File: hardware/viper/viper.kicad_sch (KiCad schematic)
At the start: 303 parts, among them J1 USB_B_Mini, Q1 2N7002, SW1 Cherry Alps Hybrid, SW10 Cherry Alps Hybrid, SW11 Cherry Alps Hybrid, SW12 Cherry Alps Hybrid, SW13 Cherry Alps Hybrid, SW14 Cherry Alps Hybrid, SW14_1 Cherry Alps Hybrid, SW15 Cherry Alps Hybrid, SW16 Cherry Alps Hybrid, SW17 Cherry Alps Hybrid, SW18 Cherry Alps Hybrid, SW19 Cherry Alps Hybrid, SW2 Cherry Alps Hybrid, SW20 Cherry Alps Hybrid, SW21 Cherry Alps Hybrid, SW22 Cherry Alps Hybrid, SW23 Cherry Alps Hybrid, SW24 Cherry Alps Hybrid, SW25 Cherry Alps Hybrid, SW26 Cherry Alps Hybrid, SW27 Cherry Alps Hybrid, SW28 Cherry Alps Hybrid, SW28_1 Cherry Alps Hybrid, SW29 Cherry Alps Hybrid, SW29_1 Cherry Alps Hybrid, SW3 Cherry Alps Hybrid, SW30 Cherry Alps Hybrid, SW31 Cherry Alps Hybrid, SW32 Cherry Alps Hybrid, SW33 Cherry Alps Hybrid, SW34 Cherry Alps Hybrid, SW35 Cherry Alps Hybrid, SW36 Cherry Alps Hybrid, SW37 Cherry Alps Hybrid, SW38 Cherry Alps Hybrid, SW39 Cherry Alps Hybrid, SW4 Cherry Alps Hybrid, SW40 Cherry Alps Hybrid, SW41 Cherry Alps Hybrid, SW41_1 Cherry Alps Hybrid, SW42 Cherry Alps Hybrid, SW43 Cherry Alps Hybrid, SW43_1 Cherry Alps Hybrid, SW44 Cherry Alps Hybrid, SW45 Cherry Alps Hybrid, SW46 Cherry Alps Hybrid, SW47 Cherry Alps Hybrid, SW48 Cherry Alps Hybrid, SW49 Cherry Alps Hybrid, SW5 Cherry Alps Hybrid, SW50 Cherry Alps Hybrid, SW51 Cherry Alps Hybrid, SW52 Cherry Alps Hybrid, SW53 Cherry Alps Hybrid, SW54 Cherry Alps Hybrid, SW55 Cherry Alps Hybrid, SW55_1 Cherry Alps Hybrid, SW56 Cherry Alps Hybrid, SW57 Cherry Alps Hybrid, SW58 Cherry Alps Hybrid, SW59 Cherry Alps Hybrid, SW6 Cherry Alps Hybrid, SW60 Cherry Alps Hybrid, SW61 Cherry Alps Hybrid, SW7 Cherry Alps Hybrid, SW8 Cherry Alps Hybrid, SW9 Cherry Alps Hybrid, U1 ATmega32U4-A, U2 PRTR5V0U2X, Y1 Crystal_GND24

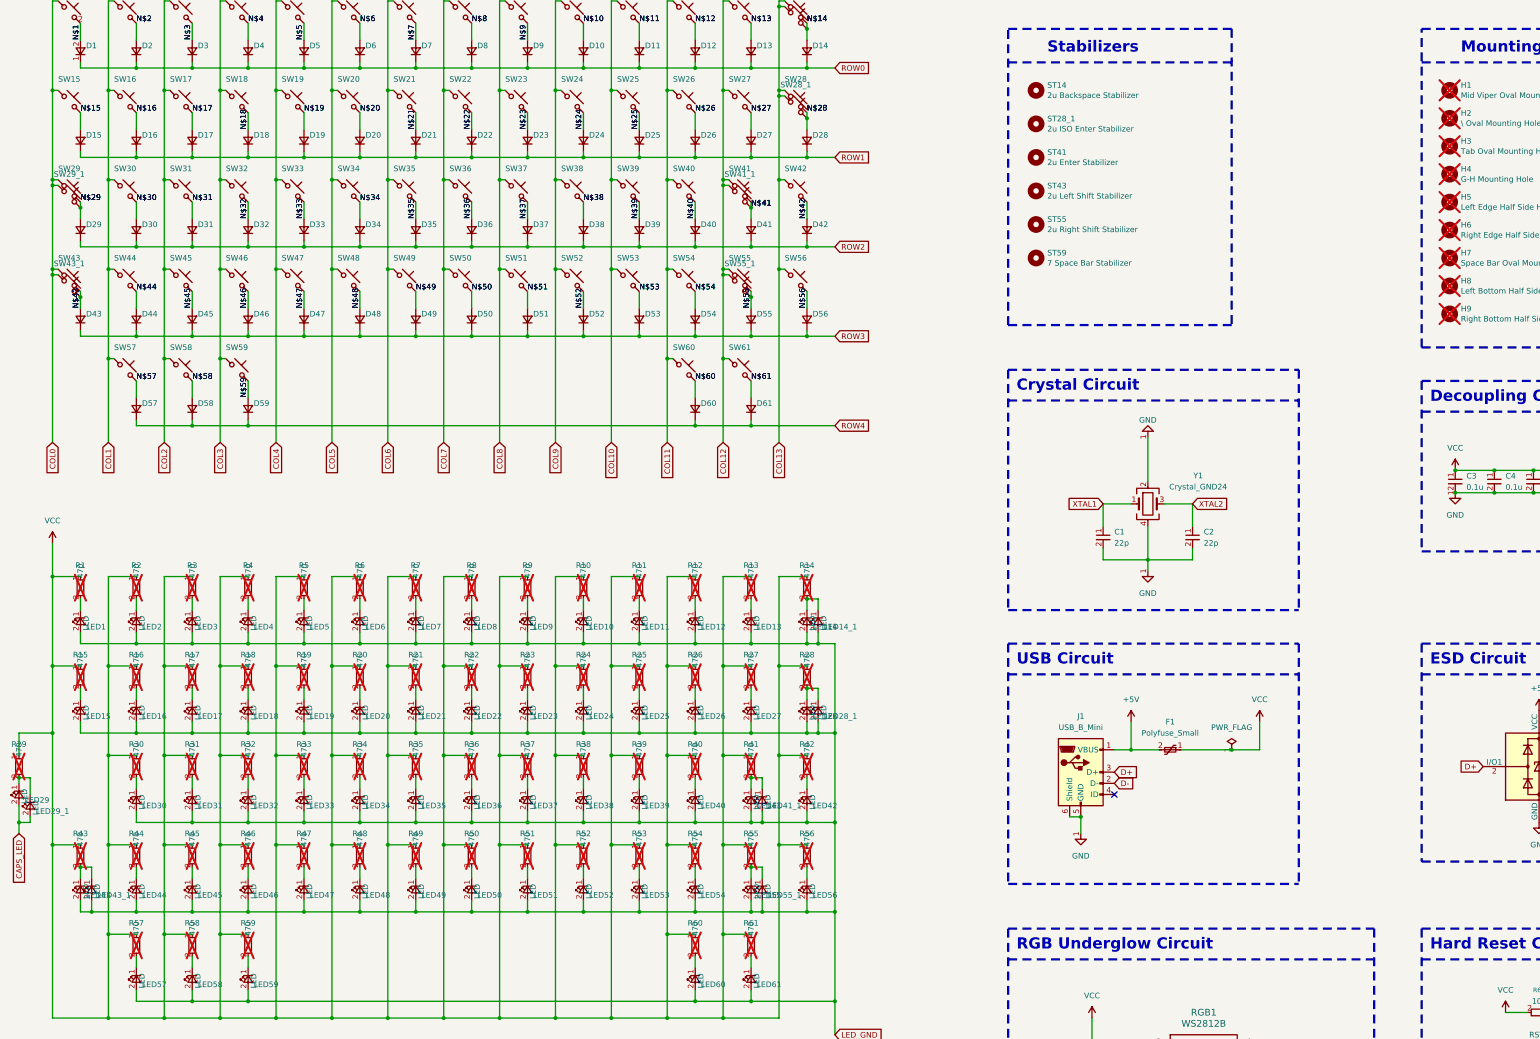
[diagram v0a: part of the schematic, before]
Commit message: Included schematic.svg in README
Removed DNP flags
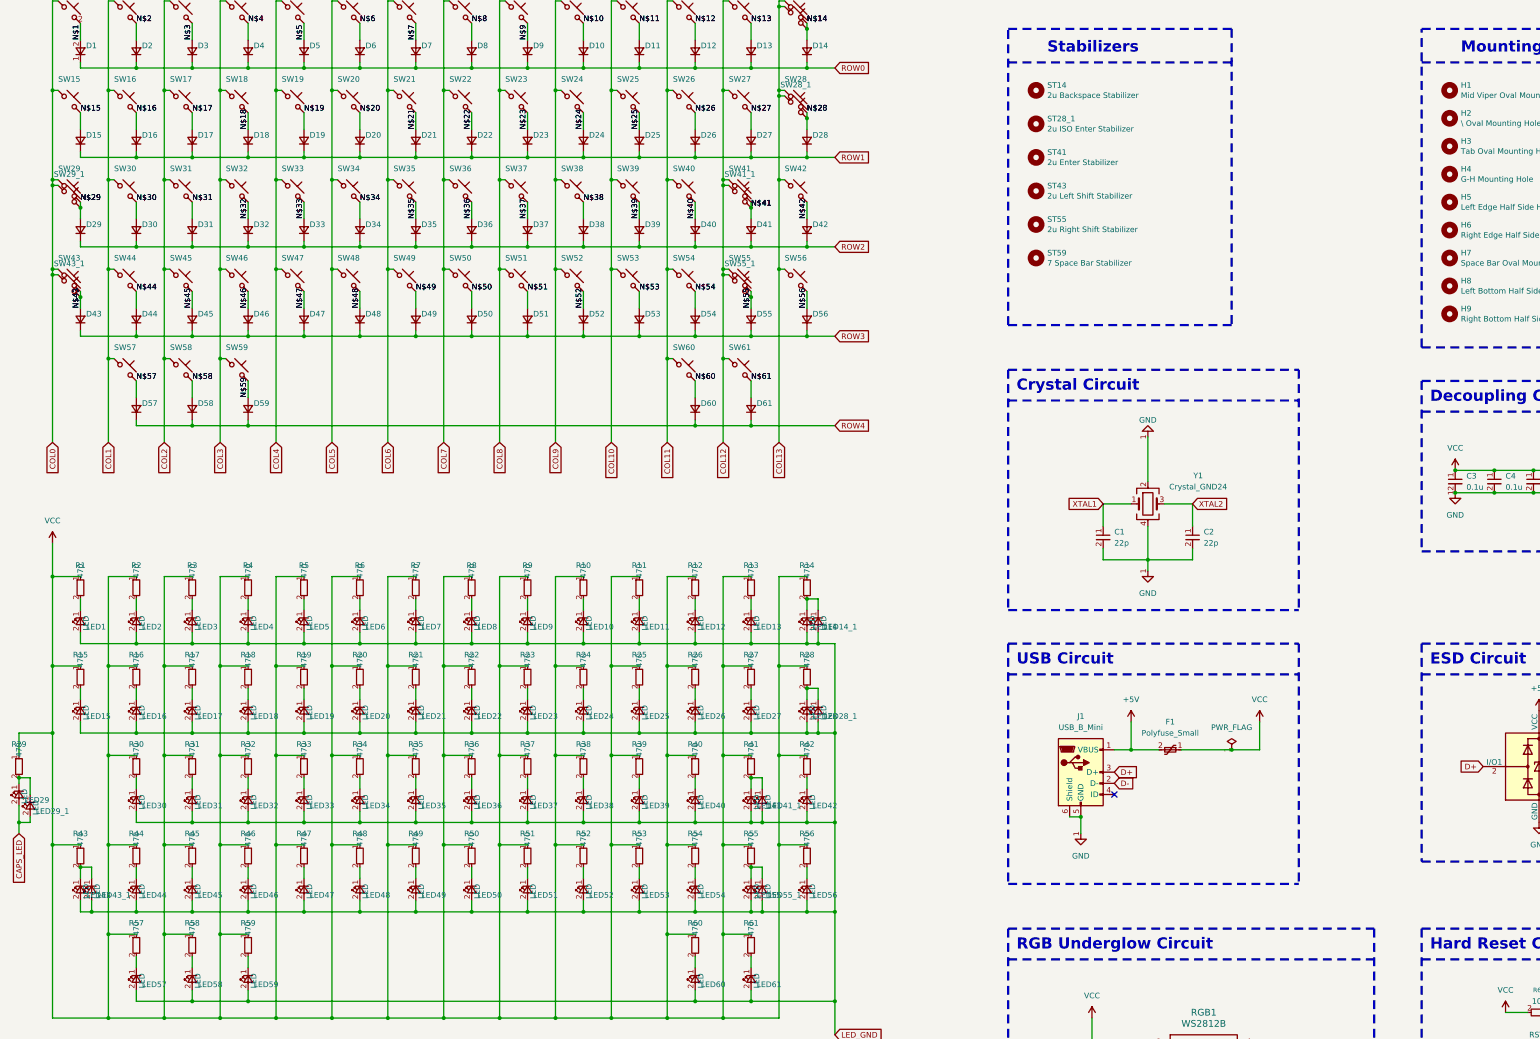
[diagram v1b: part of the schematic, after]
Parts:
- H1, H2, H3, H4, H5, H6, H7, H8, H9, R1, R10, R11, R12, R13, R14, R15, R16, R17, R18, R19, R2, R20, R21, R22, R23, R24, R25, R26, R27, R28, R29, R3, R30, R31, R32, R33, R34, R35, R36, R37, R38, R39, R4, R40, R41, R42, R43, R44, R45, R46, R47, R48, R49, R5, R50, R51, R52, R53, R54, R55, R56, R57, R58, R59, R6, R60, R61, R7, R8, R9: now fitted

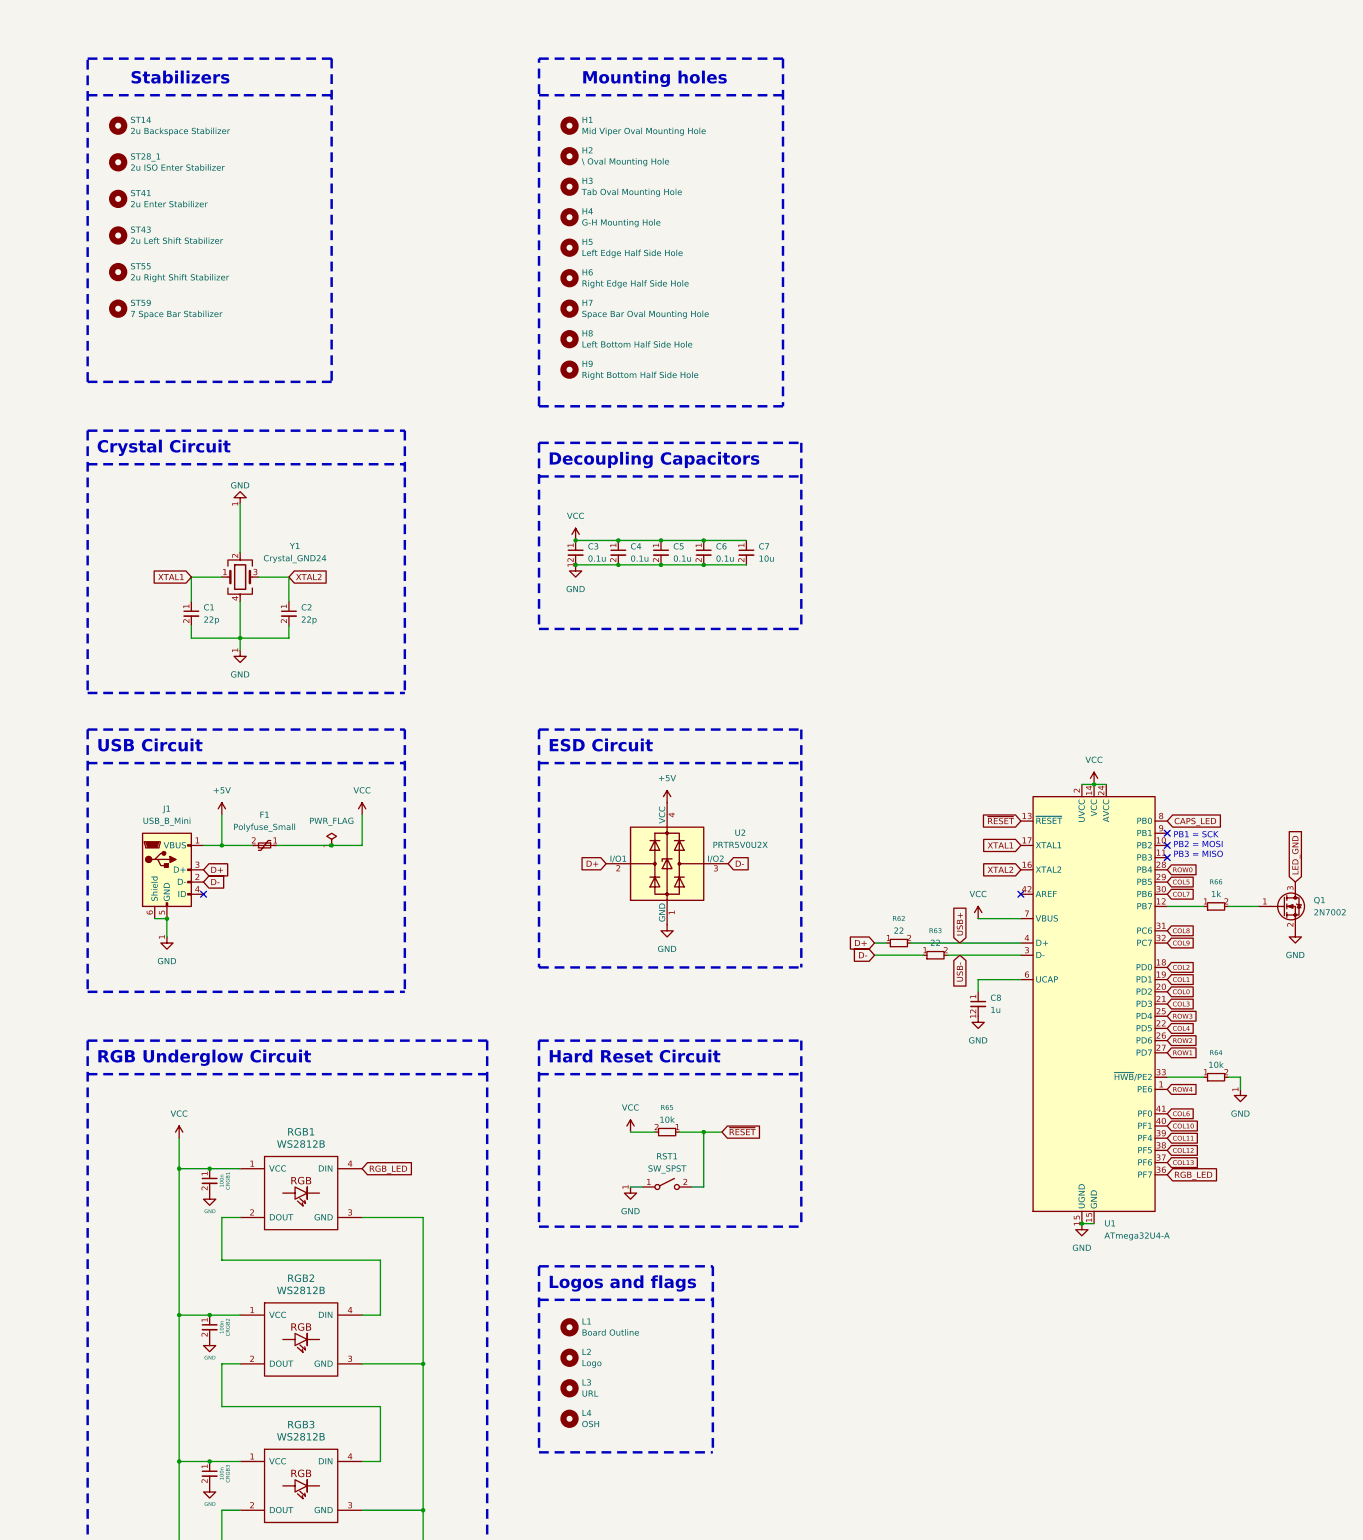
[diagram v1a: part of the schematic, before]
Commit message: Updated docs
Updated schematic & changed DSOD123F to 0805 footprints where needed
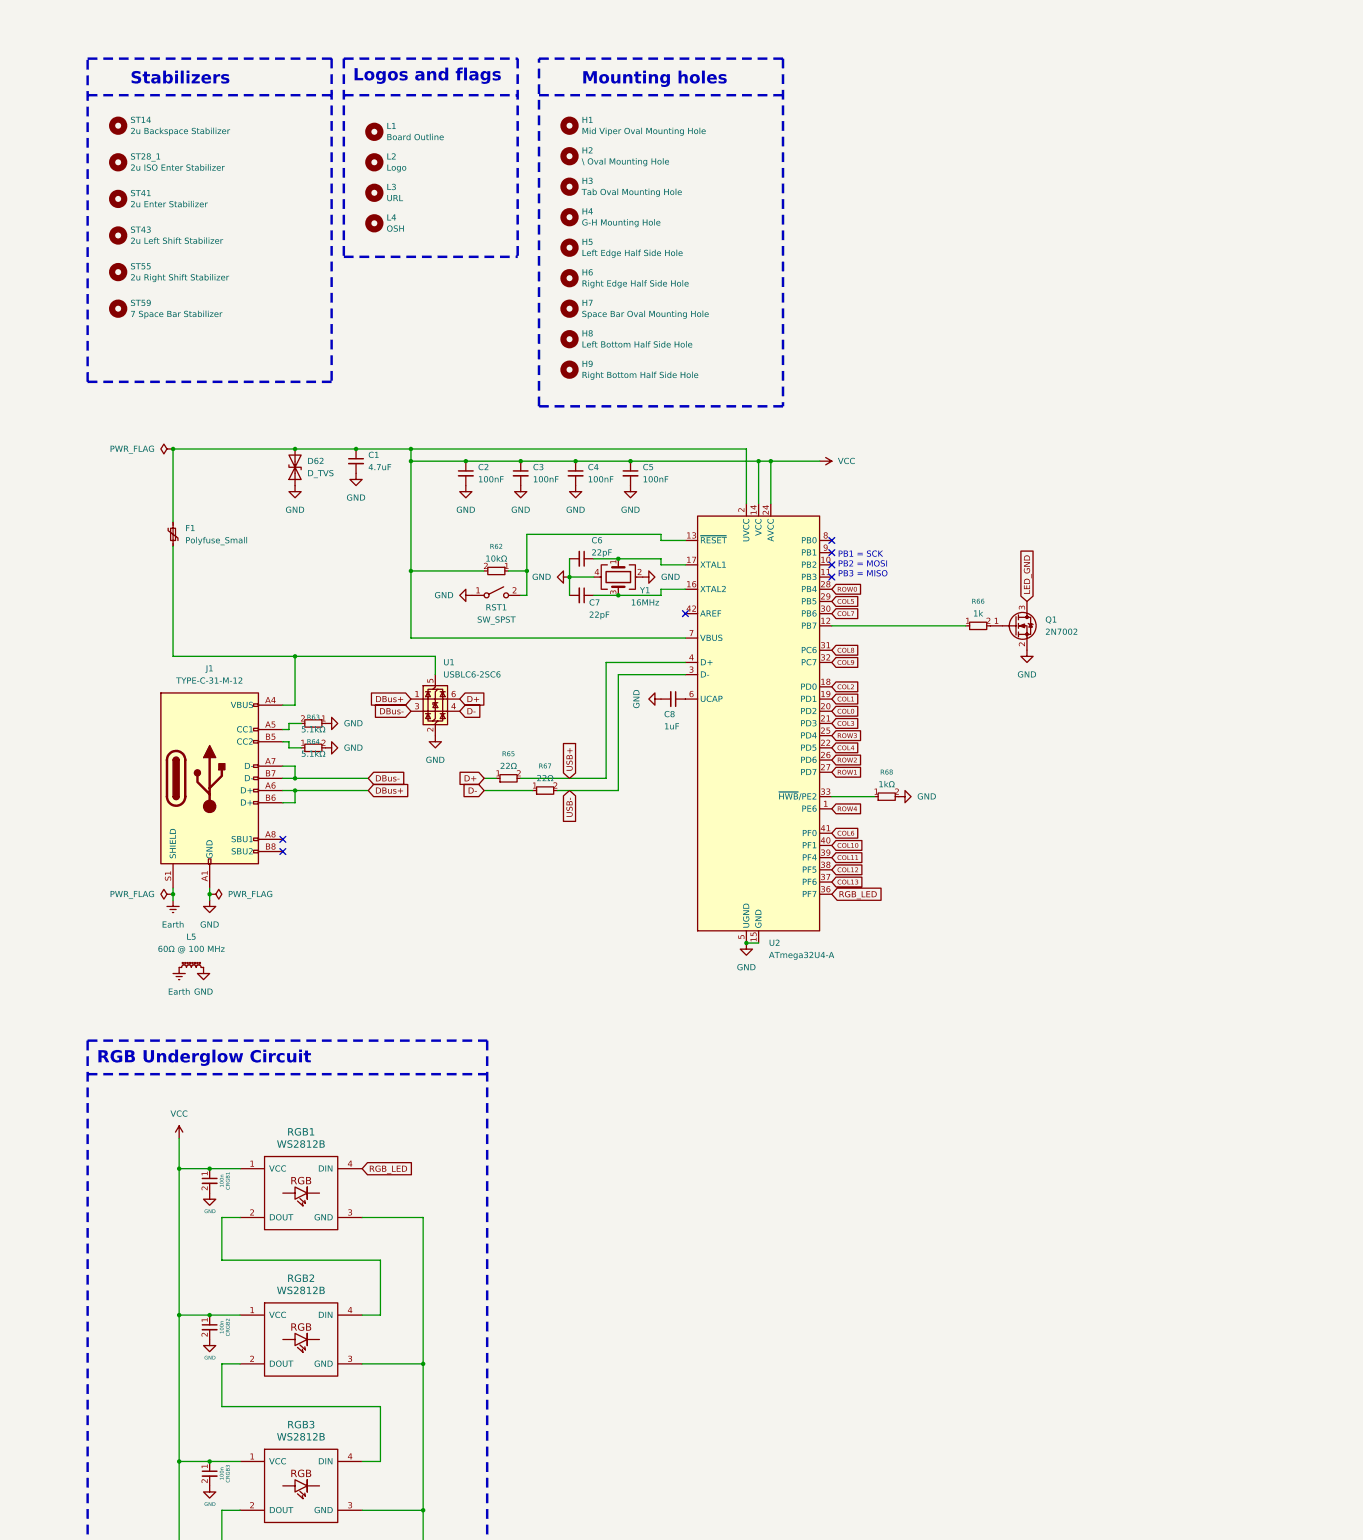
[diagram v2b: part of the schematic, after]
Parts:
- removed C2: 22p, Capacitor_SMD:C_0603_1608Metric, symbol Device:C_Small
- removed J1: USB_B_Mini, acheron_Connectors:USB_MiniB_Hirose_UX60-MB-5S8, symbol Connector:USB_B_Mini
- removed U2: PRTR5V0U2X, Package_TO_SOT_SMD:SOT-143, symbol Power_Protection:PRTR5V0U2X
- added C7: 22pF, Capacitor_SMD:C_0805_2012Metric_Pad1.18x1.45mm_HandSolder, symbol Device:C_Small
- added D62: D_TVS, Diode_SMD:D_0805_2012Metric_Pad1.15x1.40mm_HandSolder, symbol Device:D_TVS
- added J1: TYPE-C-31-M-12, Connector_USB:USB_C_Receptacle_HRO_TYPE-C-31-M-12, symbol Connector:USB_C_Receptacle_USB2.0_16P
- added L5: 60Ω @ 100 MHz, Inductor_SMD:L_1206_3216Metric_Pad1.42x1.75mm_HandSolder, symbol Device:L_Ferrite_Small
- added R67: 22Ω, Resistor_SMD:R_0805_2012Metric_Pad1.20x1.40mm_HandSolder, symbol Device:R_Small
- added R68: 1kΩ, Resistor_SMD:R_0805_2012Metric_Pad1.20x1.40mm_HandSolder, symbol Device:R_Small
- added U1: USBLC6-2SC6, Package_TO_SOT_SMD:SOT-23-6, symbol Power_Protection:USBLC6-2SC6
- C1: renamed from C3; value 0.1u -> 4.7uF; footprint Capacitor_SMD:C_0603_1608Metric -> Capacitor_SMD:C_0805_2012Metric_Pad1.18x1.45mm_HandSolder; LCSC (none) -> C36911366
- C2: renamed from C4; value 0.1u -> 100nF; footprint Capacitor_SMD:C_0603_1608Metric -> Capacitor_SMD:C_0805_2012Metric_Pad1.18x1.45mm_HandSolder; LCSC (none) -> C36911366
- C3: renamed from C5; value 0.1u -> 100nF; footprint Capacitor_SMD:C_0603_1608Metric -> Capacitor_SMD:C_0805_2012Metric_Pad1.18x1.45mm_HandSolder; LCSC (none) -> C36911366
- C4: renamed from C6; value 0.1u -> 100nF; footprint Capacitor_SMD:C_0603_1608Metric -> Capacitor_SMD:C_0805_2012Metric_Pad1.18x1.45mm_HandSolder; LCSC (none) -> C36911366
- C5: renamed from C7; value 10u -> 100nF; footprint Capacitor_SMD:C_0603_1608Metric -> Capacitor_SMD:C_0805_2012Metric_Pad1.18x1.45mm_HandSolder; LCSC (none) -> C47117445
- C6: renamed from C1; value 22p -> 22pF; footprint Capacitor_SMD:C_0603_1608Metric -> Capacitor_SMD:C_0805_2012Metric_Pad1.18x1.45mm_HandSolder; LCSC (none) -> C22399635
- C8: value 1u -> 1uF; footprint Capacitor_SMD:C_0603_1608Metric -> Capacitor_SMD:C_0805_2012Metric_Pad1.18x1.45mm_HandSolder; LCSC (none) -> C5254818
- D1, D10, D11, D12, D13, D14, D15, D16, D17, D18, D19, D2, D20, D21, D22, D23, D24, D25, D26, D27, D28, D29, D3, D30, D31, D32, D33, D34, D35, D36, D37, D38, D39, D4, D40, D41, D42, D43, D44, D45, D46, D47, D48, D49, D5, D50, D51, D52, D53, D54, D55, D56, D57, D58, D59, D6, D60, D61, D7, D8, D9: footprint Diode_SMD:D_SOD-123F -> Diode_SMD:D_0805_2012Metric_Pad1.15x1.40mm_HandSolder
- F1: footprint Fuse:Fuse_1206_3216Metric -> Fuse:Fuse_0805_2012Metric_Pad1.15x1.40mm_HandSolder; LCSC (none) -> C70158; TODO (none) -> ${ERC_ERROR TODO} Calulate proper value
- R1, R10, R11, R12, R13, R14, R15, R16, R17, R18, R19, R2, R20, R21, R22, R23, R24, R25, R26, R27, R28, R29, R3, R30, R31, R32, R33, R34, R35, R36, R37, R38, R39, R4, R40, R41, R42, R43, R44, R45, R46, R47, R48, R49, R5, R50, R51, R52, R53, R54, R55, R56, R57, R58, R59, R6, R60, R61, R7, R8, R9: footprint Resistor_SMD:R_1206_3216Metric_Pad1.30x1.75mm_HandSolder -> Resistor_SMD:R_0815_2038Metric_Pad1.20x4.05mm_HandSolder
- R62: value 22 -> 10kΩ; footprint Resistor_SMD:R_0603_1608Metric -> Resistor_SMD:R_0805_2012Metric_Pad1.20x1.40mm_HandSolder; LCSC (none) -> C17414
- R63: value 22 -> 5.1kΩ; footprint Resistor_SMD:R_0603_1608Metric -> Resistor_SMD:R_0805_2012Metric_Pad1.20x1.40mm_HandSolder; LCSC (none) -> C27834
- R64: value 10k -> 5.1kΩ; footprint Resistor_SMD:R_0603_1608Metric -> Resistor_SMD:R_0805_2012Metric_Pad1.20x1.40mm_HandSolder; LCSC (none) -> C27834
- R65: value 10k -> 22Ω; footprint Resistor_SMD:R_0603_1608Metric -> Resistor_SMD:R_0805_2012Metric_Pad1.20x1.40mm_HandSolder; LCSC (none) -> C25295
- R66: footprint Resistor_SMD:R_0603_1608Metric -> Resistor_SMD:R_0815_2038Metric_Pad1.20x4.05mm_HandSolder
- RST1: LCSC (none) -> C92584
- U2: renamed from U1; footprint Package_QFP:TQFP-44_10x10mm_P0.8mm -> Package_DFN_QFN:QFN-44-1EP_7x7mm_P0.5mm_EP5.2x5.2mm
- Y1: value Crystal_GND24 -> 16MHz; LCSC (none) -> C255909
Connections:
- net +5V is gone; now on net VCC: F1.2
- net CAPS_LED: no longer U2.8 (PB0)
- net D+: now also R65.1, U1.6 (I/O1); no longer R62.1
- net D-: now also R67.1, U1.4 (I/O2); no longer R63.1
- net GND: now also R63.1, C7.2, D62.1 (A1), J1.A1 (GND), J1.A12 (GND), J1.B1 (GND), J1.B12 (GND), L5.2, R68.2, U1.2 (GND)
- net USB+: now also R65.2; no longer R62.2
- net USB-: now also R67.2; no longer R63.2
- net VCC: now also R62.2, D62.2 (A2); no longer F1.1, R65.2
- net at R64.1: now also J1.B5 (CC2); no longer U2.33 (~{HWB}/PE2)
- net XTAL1: no longer names the net of C6.1, U2.17 (XTAL1), Y1.1
- net XTAL2: no longer names the net of U2.16 (XTAL2), Y1.3
- net XTAL2: now also C7.1
- net ~{RESET}: no longer names the net of RST1.2 (B), U2.13 (~{RESET})
- net ~{RESET}: now also R62.1; no longer R65.1
- new net: F1.1, J1.A4 (VBUS), J1.A9 (VBUS), J1.B4 (VBUS), J1.B9 (VBUS), U1.5 (VBUS)
- new net: R68.1, U2.33 (~{HWB}/PE2)
- new net: J1.A5 (CC1), R63.2
- new net DBus+: J1.A6 (D+), J1.B6 (D+), U1.1 (I/O1)
- new net DBus-: J1.A7 (D-), J1.B7 (D-), U1.3 (I/O2)
- new net Earth: J1.S1 (SHIELD), L5.1
- no-connect marks 6 -> 8
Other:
- note removed: "Crystal Circuit"
- note removed: "Decoupling Capacitors"
- note removed: "ESD Circuit"
- note removed: "Hard Reset Circuit"
- note removed: "USB Circuit"
- moved on the sheet: L1, L2, L3, L4, Q1, R66, RST1, U2, Y1

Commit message: Set value for TVS diode + fuse, keep ERC warning just in case
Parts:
- CRGB1, CRGB2, CRGB3, CRGB4: value 100n -> 100nF
- D1, D10, D11, D12, D13, D14, D15, D16, D17, D18, D19, D2, D20, D21, D22, D23, D24, D25, D26, D27, D28, D29, D3, D30, D31, D32, D33, D34, D35, D36, D37, D38, D39, D4, D40, D41, D42, D43, D44, D45, D46, D47, D48, D49, D5, D50, D51, D52, D53, D54, D55, D56, D57, D58, D59, D6, D60, D61, D7, D8, D9: value 1n4148 -> 1N4148
- D62: value D_TVS -> SMF9.0CA
- F1: value Polyfuse_Small -> 1.5A trip PTC
- R1, R10, R11, R12, R13, R14, R15, R16, R17, R18, R19, R2, R20, R21, R22, R23, R24, R25, R26, R27, R28, R29, R3, R30, R31, R32, R33, R34, R35, R36, R37, R38, R39, R4, R40, R41, R42, R43, R44, R45, R46, R47, R48, R49, R5, R50, R51, R52, R53, R54, R55, R56, R57, R58, R59, R6, R60, R61, R7, R8, R9: value 470 -> 470Ω
- R66: value 1k -> 1kΩ
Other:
- moved on the sheet: Q1, R66
